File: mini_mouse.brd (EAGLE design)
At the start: 160 x 100 mm, 33 parts, among them IC1 PIC18F4550_TQFP, IC2 L298, IC3 LP2950CDT-5.0

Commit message: Cambios finales a esquemático, inicio de board
Se realizaron los ultimos cambios al esquemático. Se empezó el diseño del pcb
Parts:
- removed IC2: L298, st-microelectronics:MULTIWATT-15
- removed JP1: (no value), pinhead:1X02
- added IC4: L293D, st-microelectronics:DIL16
- moved C4 157.2 mm to (19.1, 83.8), flipped to the bottom
- moved ALIMENTACIÓN 133.0 mm to (76.2, 3.81), turned to 180 degrees
- moved ACTIVADOR 131.2 mm to (3.81, 74.9), turned to 90 degrees
- moved JP2 126.6 mm to (64.0, 5.03), turned to 180 degrees
- moved COMUNICACIÓN 119.4 mm to (82.4, 69.6), turned to 90 degrees
- moved IC1 98.3 mm to (46.0, 46.0), flipped to the bottom, turned to 45 degrees
- moved SENSOR1 92.7 mm to (30.5, 33.0)
- moved ENCODER_2 90.8 mm to (66.0, 72.0), turned to 90 degrees
- moved IC3 90.2 mm to (69.8, 21.6), flipped to the bottom, turned to 90 degrees
- moved ENCODER_1 82.3 mm to (26.0, 72.0), turned to 270 degrees
- moved Q1 57.1 mm to (35.6, 57.3), turned to 45 degrees
- moved OPCIONES 55.8 mm to (3.81, 64.8), turned to 180 degrees
- moved C2 52.5 mm to (33.4, 61.8), flipped to the bottom
- moved PROG 46.0 mm to (3.81, 26.7), turned to 270 degrees
- moved C1 44.9 mm to (29.2, 57.1), flipped to the bottom
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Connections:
- net +5V: no longer IC2.9
- net BAT: now also IC4.16, IC4.8; no longer IC2.4
- net D1_M1: now also IC4.2; no longer IC2.5
- net D1_M2: now also IC4.15; no longer IC2.10
- net D2_M1: now also IC4.7; no longer IC2.7
- net D2_M2: now also IC4.10; no longer IC2.12
- net GND: now also IC4.12, IC4.13, IC4.4, IC4.5; no longer IC2.8, JP1.2
- net M1_1: now also IC4.3; no longer IC2.3
- net M1_2: now also IC4.14; no longer IC2.14
- net M2_1: now also IC4.6; no longer IC2.2
- net M2_2: now also IC4.11; no longer IC2.13
- net N$5: no longer JP1.1
- net PWM_1: now also IC4.1; no longer IC2.6
- net PWM_2: now also IC4.9; no longer IC2.11
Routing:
- net BAT: track 0.00 -> 205.6 mm
- net D1_M2: track 0.00 -> 79.0 mm
- net +5V: track 0.00 -> 65.6 mm, vias 0 -> 2
- net TX: track 0.00 -> 43.5 mm
- net RX: track 0.00 -> 43.4 mm
- net D1_M1: track 0.00 -> 39.8 mm, vias 0 -> 2
- net D2_M2: track 0.00 -> 39.0 mm
- net D2_M1: track 0.00 -> 30.1 mm, vias 0 -> 2
- net PWM_2: track 0.00 -> 29.0 mm
- net M1_2: track 0.00 -> 28.1 mm
- net PWM_1: track 0.00 -> 23.3 mm
- net M2_2: track 0.00 -> 20.3 mm
- net N$5: track 0.00 -> 16.7 mm
- net OSC1: track 0.00 -> 15.4 mm
- net OSC2: track 0.00 -> 14.0 mm
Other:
- board size 160 x 100 mm -> 92 x 92 mm

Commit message: pcb
Se realizò PCB en un 90%
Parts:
- C3, C4: device rcl:153CLV-0405 -> rcl:E5-6
- moved C3 160.5 mm to (81.6, 22.6), turned to 180 degrees
- moved RS3 141.8 mm to (9.19, 78.4), flipped to the bottom
- moved SENSOR4 117.3 mm to (31.6, 56.7)
- moved SENSOR3 117.2 mm to (31.6, 62.9)
- moved SENSOR2 116.7 mm to (31.7, 68.5)
- moved LED5 99.3 mm to (36.1, 88.7)
- moved LED4 95.8 mm to (42.5, 88.7)
- moved LED3 92.7 mm to (49.5, 88.6)
- moved LED2 90.1 mm to (56.7, 88.8)
- moved R_L1 86.4 mm to (56.5, 83.2), flipped to the bottom
- moved R_L2 85.7 mm to (49.4, 83.3), flipped to the bottom
- moved R_L4 85.5 mm to (36.4, 83.4), flipped to the bottom
- moved R_L3 85.4 mm to (42.6, 83.4), flipped to the bottom
- moved C4 81.8 mm to (81.4, 30.8), flipped to the top
- moved RS2 64.1 mm to (8.23, 61.1), flipped to the bottom
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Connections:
- net D1_M1: now also IC1.23; no longer IC1.43
- net D1_M2: now also IC1.15; no longer IC1.41
- net D2_M1: now also IC1.24; no longer IC1.42
- net D2_M2: now also IC1.14; no longer IC1.40
- net LED_1: now also IC1.43
- net LED_2: now also IC1.42
- net LED_3: now also IC1.41
- net LED_4: now also IC1.40
- net M1_2: now also IC4.11; no longer IC4.14
- net M2_2: now also IC4.14; no longer IC4.11
- net OUT_B1: now also IC1.11; no longer IC1.10
- net OUT_B2: now also IC1.10; no longer IC1.11
- net PWM_1: now also IC1.35; no longer IC1.36
- net PWM_2: now also IC1.36; no longer IC1.35
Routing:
- net +5V: track 65.6 -> 366.9 mm, vias 2 -> 0
- net BAT: track 205.6 -> 105.2 mm
- net PWM_1: track 23.3 -> 101.8 mm
- net D2_M1: track 30.1 -> 102.6 mm
- net D1_M2: track 79.0 -> 19.9 mm, vias 0 -> 2
- net S1: track 0.00 -> 49.7 mm
- net PWM_2: track 29.0 -> 78.3 mm
- net LED_4: track 0.00 -> 48.2 mm, vias 0 -> 2
- net LED_3: track 0.00 -> 46.3 mm, vias 0 -> 2
- net M2_1: track 0.00 -> 45.0 mm
- net LED_1: track 0.00 -> 44.5 mm, vias 0 -> 2
- net LED_2: track 0.00 -> 44.2 mm, vias 0 -> 2
- net D1_M1: track 39.8 -> 80.4 mm, vias 2 -> 4
- net S2: track 0.00 -> 40.5 mm
- net OUT_A1: track 0.00 -> 33.4 mm
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
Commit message: Ajuste PCB
Se realizó el ajuste del pcb
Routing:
- net +5V: track 366.9 -> 366.0 mm
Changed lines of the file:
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@@
 <wire x1="5.08" y1="73.66" x2="17.1958" y2="73.66" width="0.508" layer="16"/>
 <wire x1="17.1958" y1="73.66" x2="21.2598" y2="77.724" width="0.508" layer="16"/>
-<wire x1="21.5646" y1="69.2912" x2="21.5646" y2="58.3692" width="0.508" layer="16"/>
-<wire x1="21.5646" y1="58.3692" x2="21.5646" y2="41.6052" width="0.508" layer="16"/>
+<wire x1="21.5646" y1="69.2912" x2="21.5646" y2="57.4548" width="0.508" layer="16"/>
+<wire x1="21.5646" y1="57.4548" x2="21.5646" y2="41.6052" width="0.508" layer="16"/>
 <wire x1="21.5646" y1="41.6052" x2="21.5646" y2="33.251" width="0.508" layer="16"/>
 <wire x1="21.5646" y1="69.2912" x2="17.1958" y2="73.66" width="0.508" layer="16"/>
@@
 <wire x1="87.1728" y1="8.6868" x2="83.8962" y2="8.6868" width="0.6096" layer="16"/>
 <wire x1="83.8962" y1="8.6868" x2="78.0288" y2="2.8194" width="0.6096" layer="16"/>
-<wire x1="21.5646" y1="57.7596" x2="15.1638" y2="51.3588" width="0.6096" layer="16"/>
-<wire x1="21.5646" y1="57.7596" x2="21.5646" y2="58.3692" width="0.6096" layer="16"/>
 <wire x1="89.7636" y1="30.9372" x2="89.7636" y2="11.2776" width="0.6096" layer="16"/>
 <wire x1="89.7636" y1="11.2776" x2="87.1728" y2="8.6868" width="0.6096" layer="16"/>
@@
 <wire x1="26" y1="29.73" x2="25.0856" y2="29.73" width="0.508" layer="16"/>
 <wire x1="25.0856" y1="29.73" x2="21.5646" y2="33.251" width="0.508" layer="16"/>
-<wire x1="15.1638" y1="51.3588" x2="15.1638" y2="42.5958" width="0.508" layer="16"/>
+<wire x1="15.1638" y1="51.054" x2="15.1638" y2="42.5958" width="0.508" layer="16"/>
 <wire x1="17.612" y1="40.1476" x2="17.612" y2="35.6714" width="0.508" layer="16"/>
 <wire x1="15.1638" y1="42.5958" x2="17.612" y2="40.1476" width="0.508" layer="16"/>
@@
 <wire x1="14.9733" y1="33.0327" x2="14.9733" y2="14.8971" width="0.508" layer="16"/>
 <wire x1="14.9733" y1="14.8971" x2="27.051" y2="2.8194" width="0.508" layer="16"/>
+<wire x1="15.1638" y1="51.054" x2="21.5646" y2="57.4548" width="0.508" layer="16"/>
 </signal>
 <signal name="PGD">

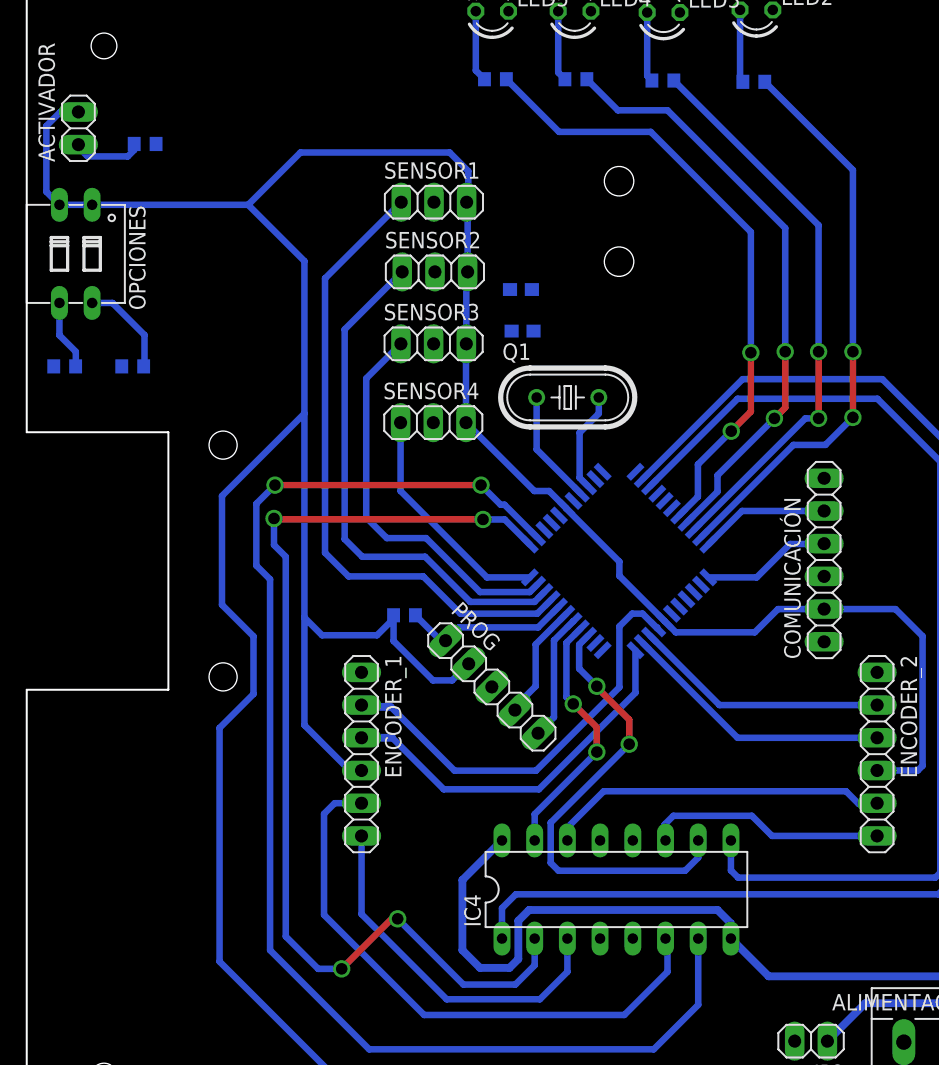
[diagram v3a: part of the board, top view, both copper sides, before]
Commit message: Pads correctos
Se agregaron los pads deseados y se terminaron de cablear componentes faltantes
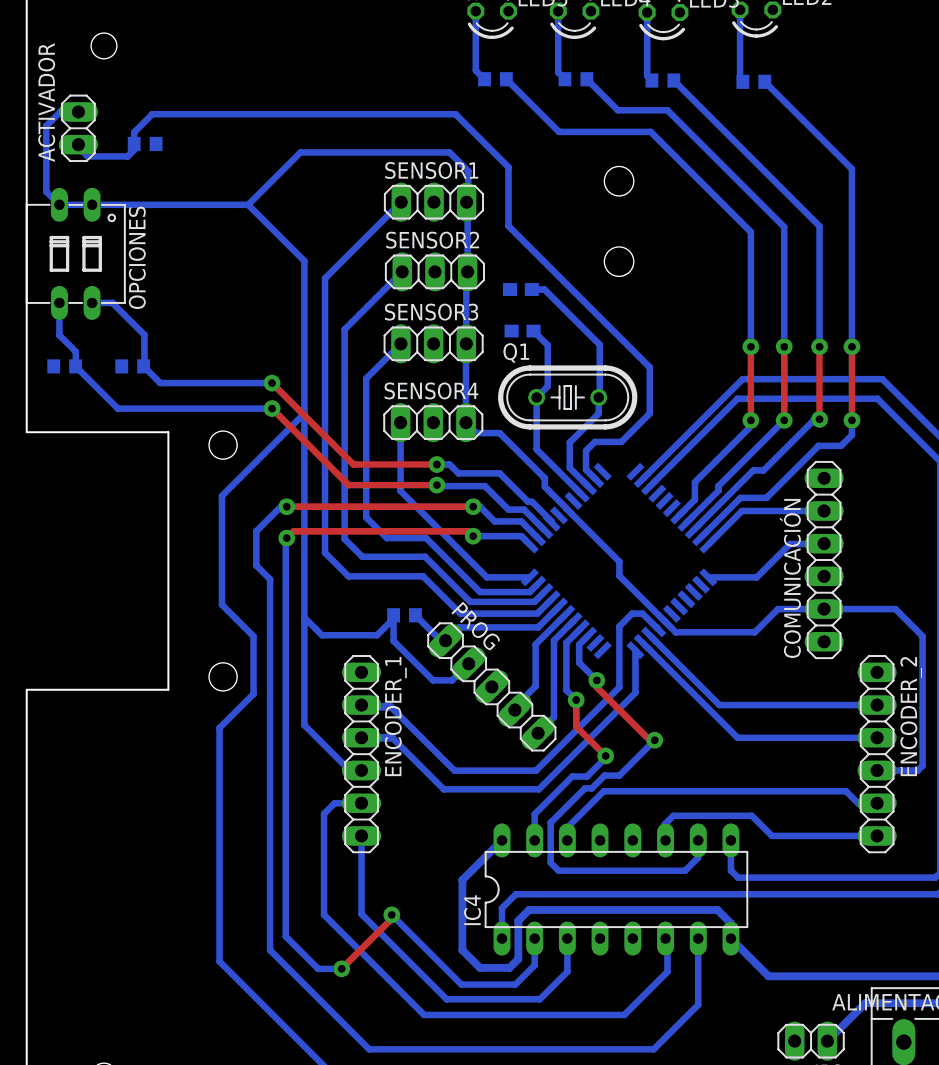
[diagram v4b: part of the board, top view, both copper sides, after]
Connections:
- net PA_1: now also IC1.25; no longer IC1.27
- net START: now also IC1.32; no longer IC1.25
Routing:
- net START: track 5.50 -> 70.1 mm
- net PA_1: track 5.46 -> 47.1 mm, vias 0 -> 2
- net PA_2: track 7.56 -> 44.3 mm, vias 0 -> 2
- net OSC2: track 7.97 -> 19.8 mm
- net OSC1: track 8.89 -> 15.2 mm
- net D2_M1: track 102.6 -> 99.6 mm
- net D2_M2: track 35.6 -> 38.4 mm
- net D1_M1: track 80.4 -> 77.7 mm
- net D1_M2: track 19.9 -> 21.1 mm
- net LED_1: track 44.5 -> 45.2 mm

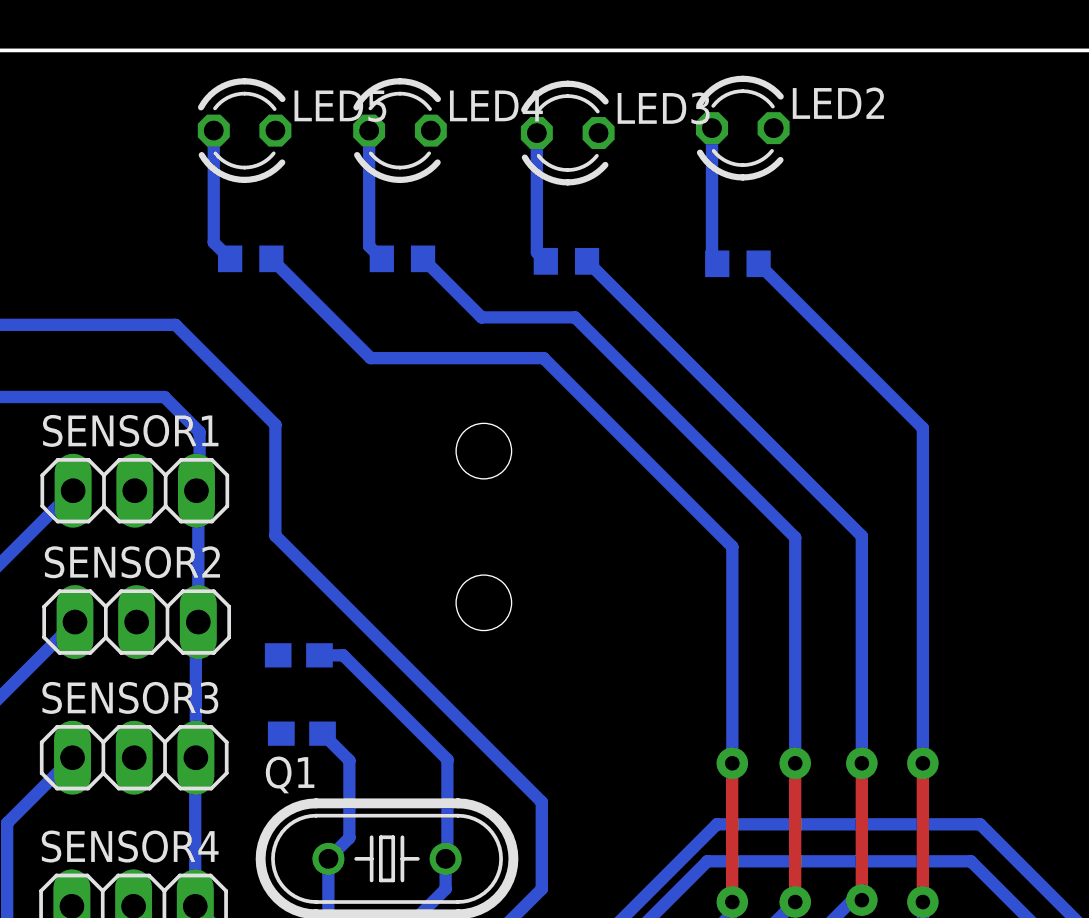
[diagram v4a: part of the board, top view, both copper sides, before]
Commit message: Acomodo de leds
Se centraron los leds
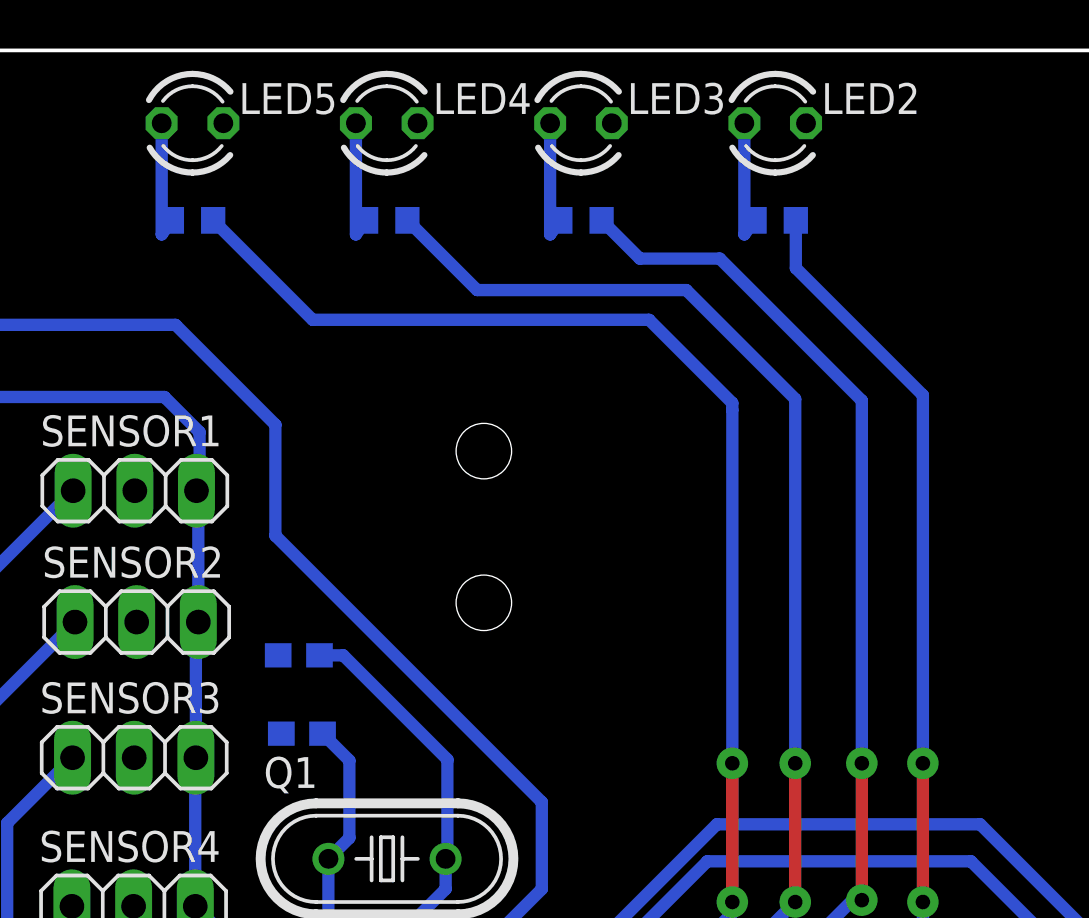
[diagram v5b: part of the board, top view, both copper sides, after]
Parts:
- moved R_L4 2.88 mm to (34.0, 85.0)
- moved R_L1 2.36 mm to (58.0, 85.0)
- moved LED5 2.17 mm to (34.0, 89.0)
- moved R_L2 1.79 mm to (50.0, 85.0)
- moved R_L3 1.71 mm to (42.0, 85.0)
- moved LED2 1.35 mm to (58.0, 89.0)
- moved LED3 0.68 mm to (50.0, 89.0)
- moved LED4 0.62 mm to (42.0, 89.0)
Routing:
- net LED_4: track 48.2 -> 54.7 mm
- net LED_3: track 46.2 -> 50.8 mm, vias 2 -> 3
- net LED_2: track 44.3 -> 47.7 mm
- net LED_1: track 45.2 -> 46.4 mm
